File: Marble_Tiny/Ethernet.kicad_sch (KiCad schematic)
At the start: 40 parts, among them J3 BELFUSE_0826-1G1T-43-F, Q1 XTAL_25MHZ_EPSON_TSX-3225_25.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, U7 RTL8211F-CG

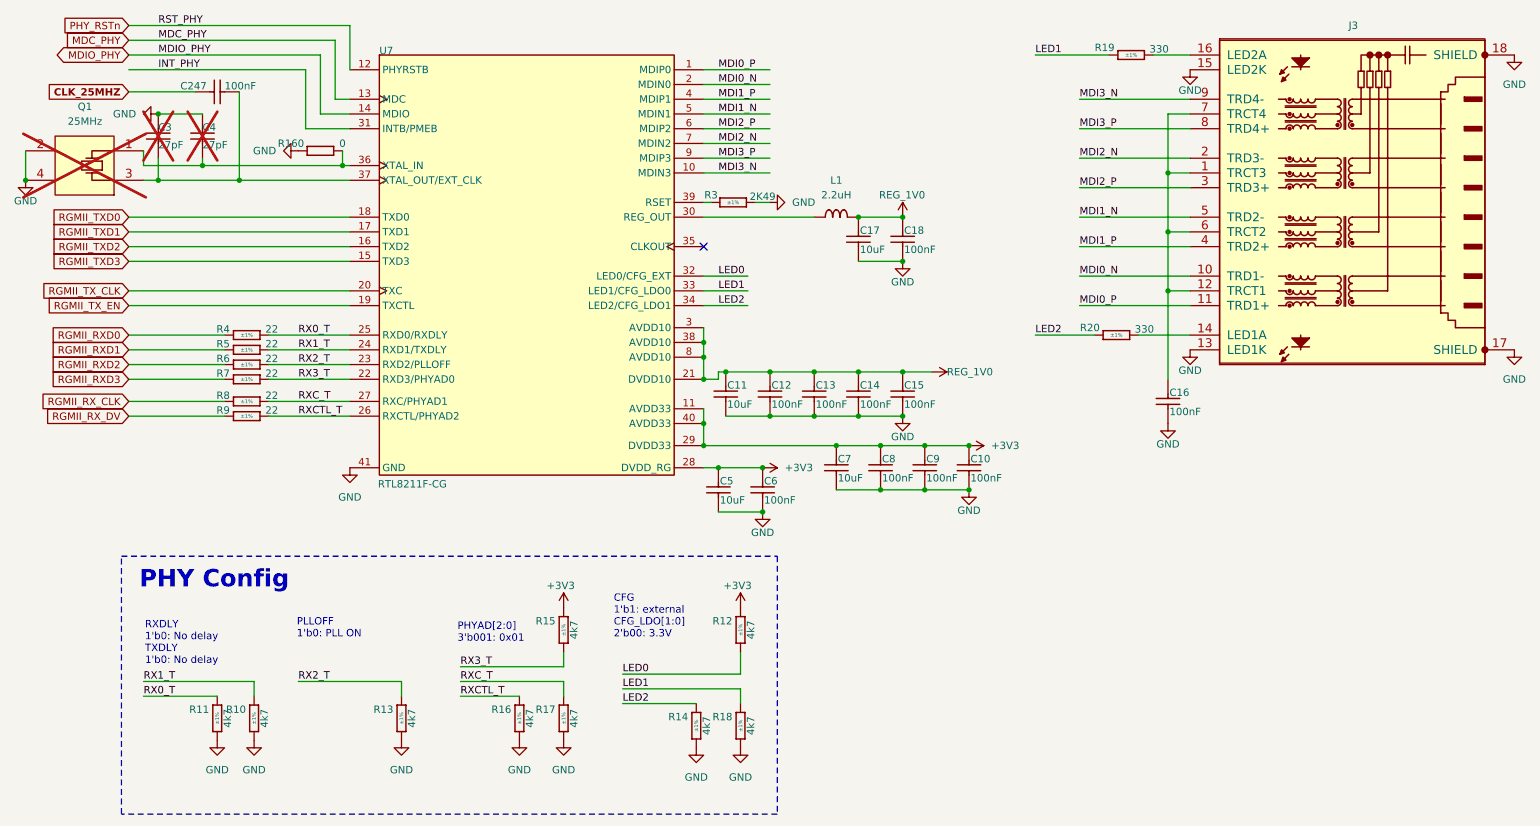
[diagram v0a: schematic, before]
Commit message: fixed ERCs; added test points; added WP switch
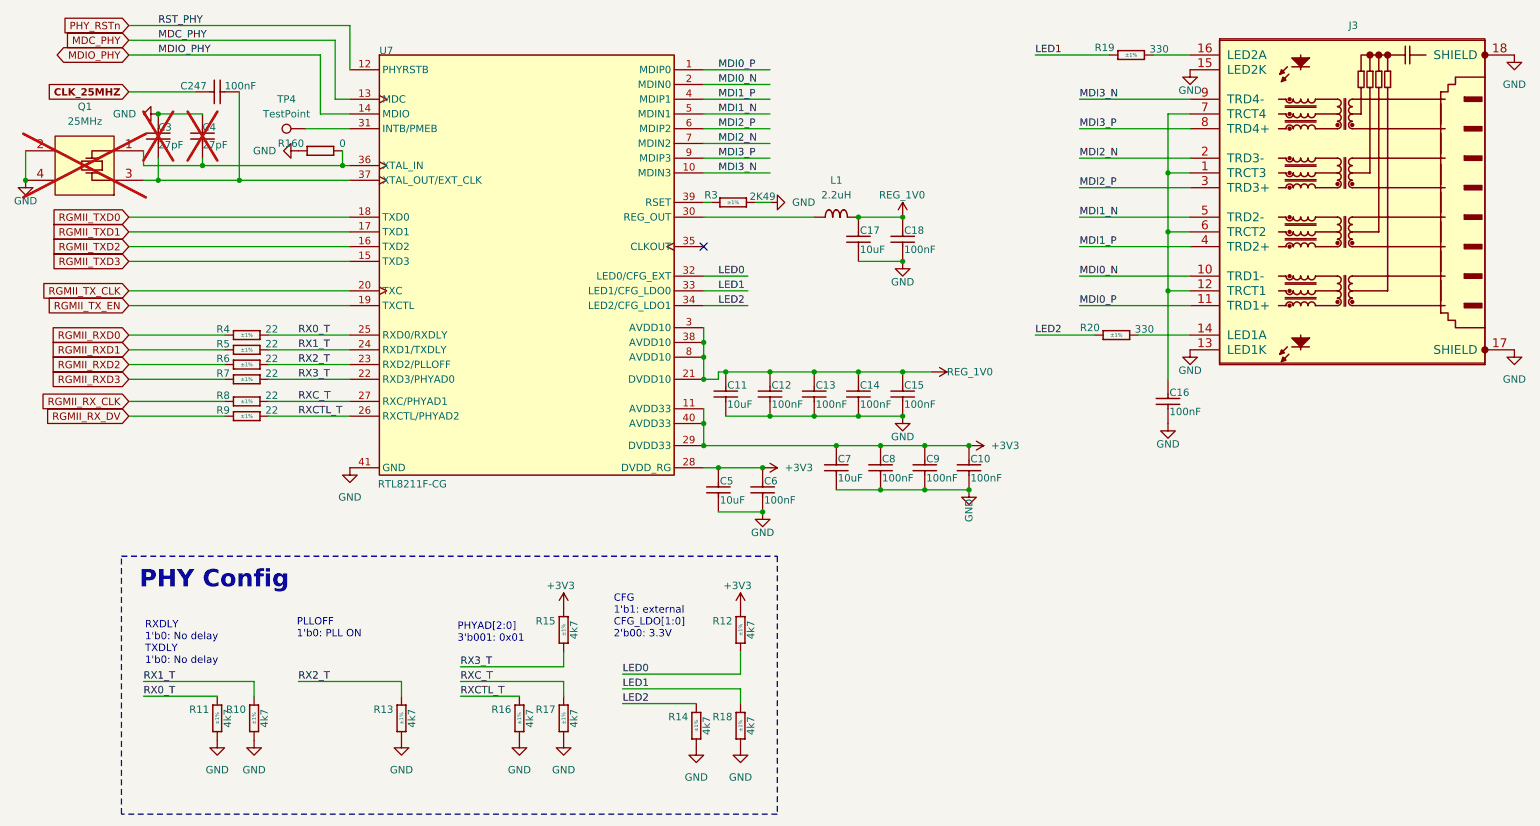
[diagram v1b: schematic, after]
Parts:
- added TP4: TestPoint, TestPoint:TestPoint_Pad_D1.5mm, symbol Connector:TestPoint
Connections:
- net INT_PHY: no longer names the net of U7.31 (INTB/PMEB)
- net INT_PHY: now also TP4.1
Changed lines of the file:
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@@
 	(wire
 		(pts
-			(xy 77.47 62.23) (xy 69.85 62.23)
-		)
-		(stroke
-			(width 0)
-			(type default)
-		)
-	)
-	(wire
-		(pts
 			(xy 218.44 80.01) (xy 218.44 90.17)
 		)
@@
 	(wire
 		(pts
-			(xy 39.37 52.07) (xy 69.85 52.07)
-		)
-		(stroke
-			(width 0)
-			(type default)
-		)
-	)
-	(wire
-		(pts
 			(xy 203.2 92.71) (xy 222.25 92.71)
 		)
@@
 	(wire
 		(pts
+			(xy 69.85 62.23) (xy 77.47 62.23)
+		)
+		(stroke
+			(width 0)
+			(type default)
+		)
+	)
+	(wire
+		(pts
 			(xy 142.24 111.76) (xy 149.86 111.76)
 		)
@@
 	(wire
 		(pts
-			(xy 69.85 62.23) (xy 69.85 52.07)
-		)
-		(stroke
-			(width 0)
-			(type default)
-		)
-	)
-	(wire
-		(pts
 			(xy 96.52 160.02) (xy 106.68 160.02)
 		)
@@
 		)
 	)
-	(label "INT_PHY"
-		(at 44.45 52.07 0)
-		(effects
-			(font
-				(size 1.27 1.27)
-			)
-			(justify left bottom)
-		)
-	)
 	(label "MDI3_P"
 		(at 140.97 67.31 0)
@@
 		)
 		(property "Value" "GND"
-			(at 184.15 128.016 0)
+			(at 184.15 128.016 90)
 			(effects
 				(font
@@
 					(unit 1)
 				)
+			)
+		)
+	)
+	(symbol
+		(lib_id "Connector:TestPoint")
+		(at 69.85 62.23 90)
+		(unit 1)
+		(exclude_from_sim no)
+		(in_bom yes)
+		(on_board yes)
+		(dnp no)
+		(fields_autoplaced yes)
+		(property "Reference" "TP4"
+			(at 66.548 57.15 90)
+			(effects
+				(font
+					(size 1.27 1.27)
+				)
+			)
+		)
+		(property "Value" "TestPoint"
+			(at 66.548 59.69 90)
+			(effects
+				(font
+					(size 1.27 1.27)
+				)
+			)
+		)
+		(property "Footprint" "TestPoint:TestPoint_Pad_D1.5mm"
+			(at 69.85 57.15 0)
+			(effects
+				(font
+					(size 1.27 1.27)
+				)
+				(hide yes)
+			)
+		)
+		(property "Datasheet" "~"
+			(at 69.85 57.15 0)
+			(effects
+				(font
+					(size 1.27 1.27)
+				)
+				(hide yes)
+			)
+		)
+		(property "Description" "test point"
+			(at 69.85 62.23 0)
+			(effects
+				(font
+					(size 1.27 1.27)
+				)
+				(hide yes)
+			)
+		)
+		(pin "1"
+		)
+		(instances
+			(project ""
+				(path "/c2a4f786-b14c-434a-acf7-b20fb2221b0b/41baefe0-2999-4159-91c6-ae67dbf0b6a8"
+					(reference "TP4")
+					(unit 1)
+				)

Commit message: fixed issue with PMODs; added board name and revision; fixed polygons issue
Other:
- company: (none) -> ${name}
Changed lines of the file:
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@@
 	(generator_version "9.0")
 	(paper "A4")
+	(title_block
+		(date "2025-04-18")
+		(rev "${rev}")
+		(company "${name}")
+		(comment 1 "${author}")
+	)
 	(bus_alias "RGMII"
 		(members "RX0" "RX1" "RX2" "RX3" "RXC" "RXCTL" "TX0" "TX1" "TX2" "TX3"
